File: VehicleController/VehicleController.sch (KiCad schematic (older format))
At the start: 20 parts, among them P2 BATT_IN, U1 Teensy_3.5

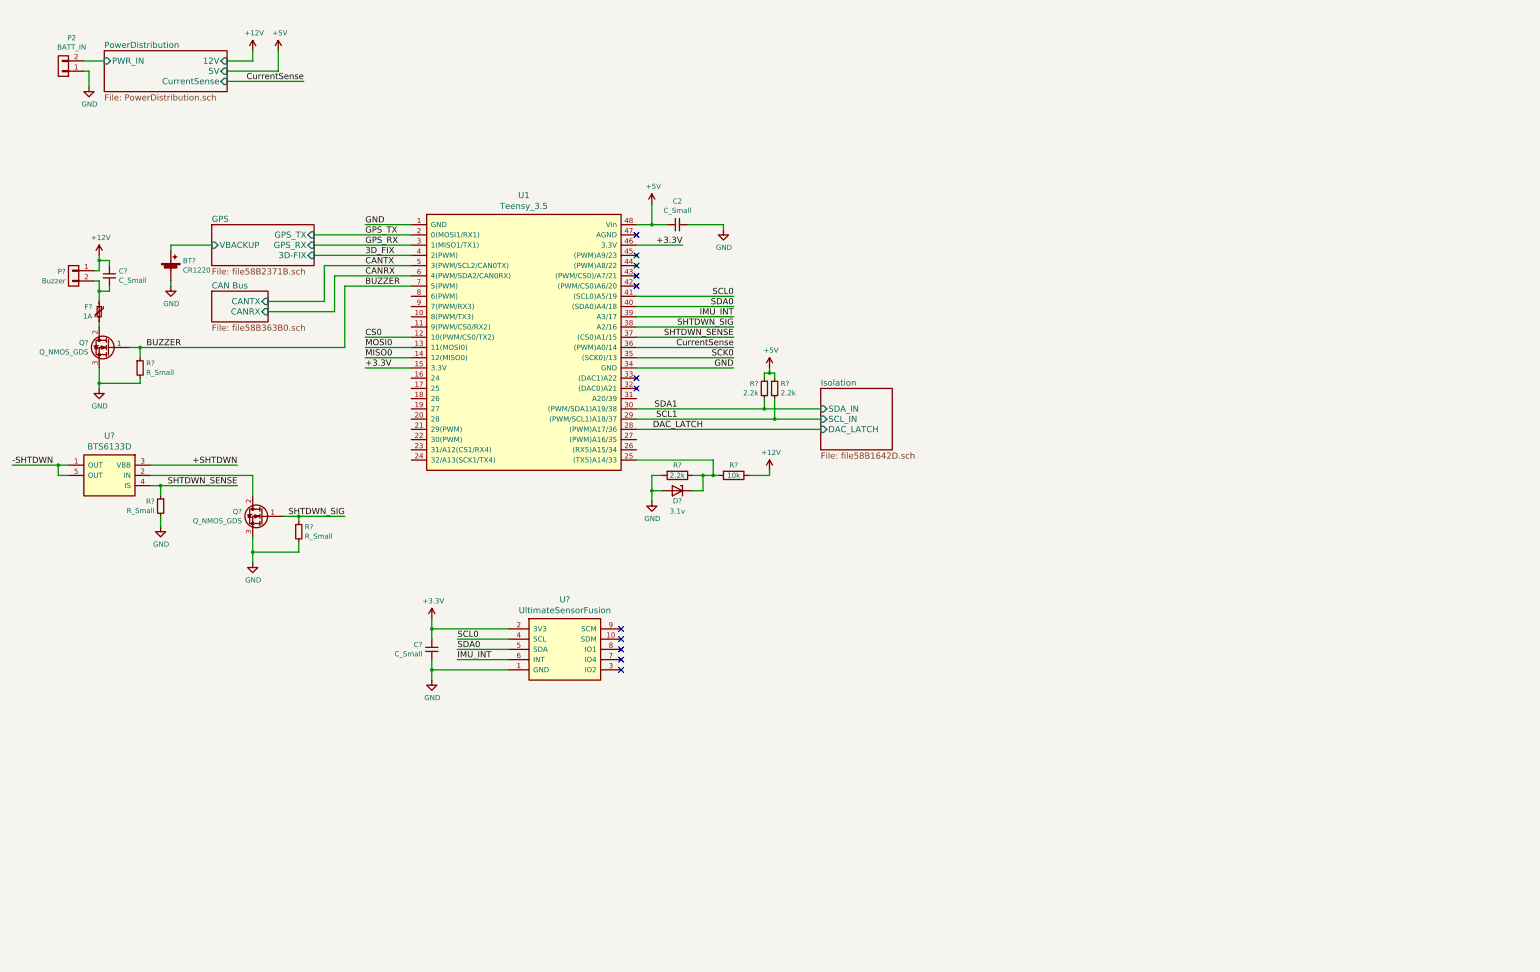
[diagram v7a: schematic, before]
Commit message: Add High-G Accel, connectors
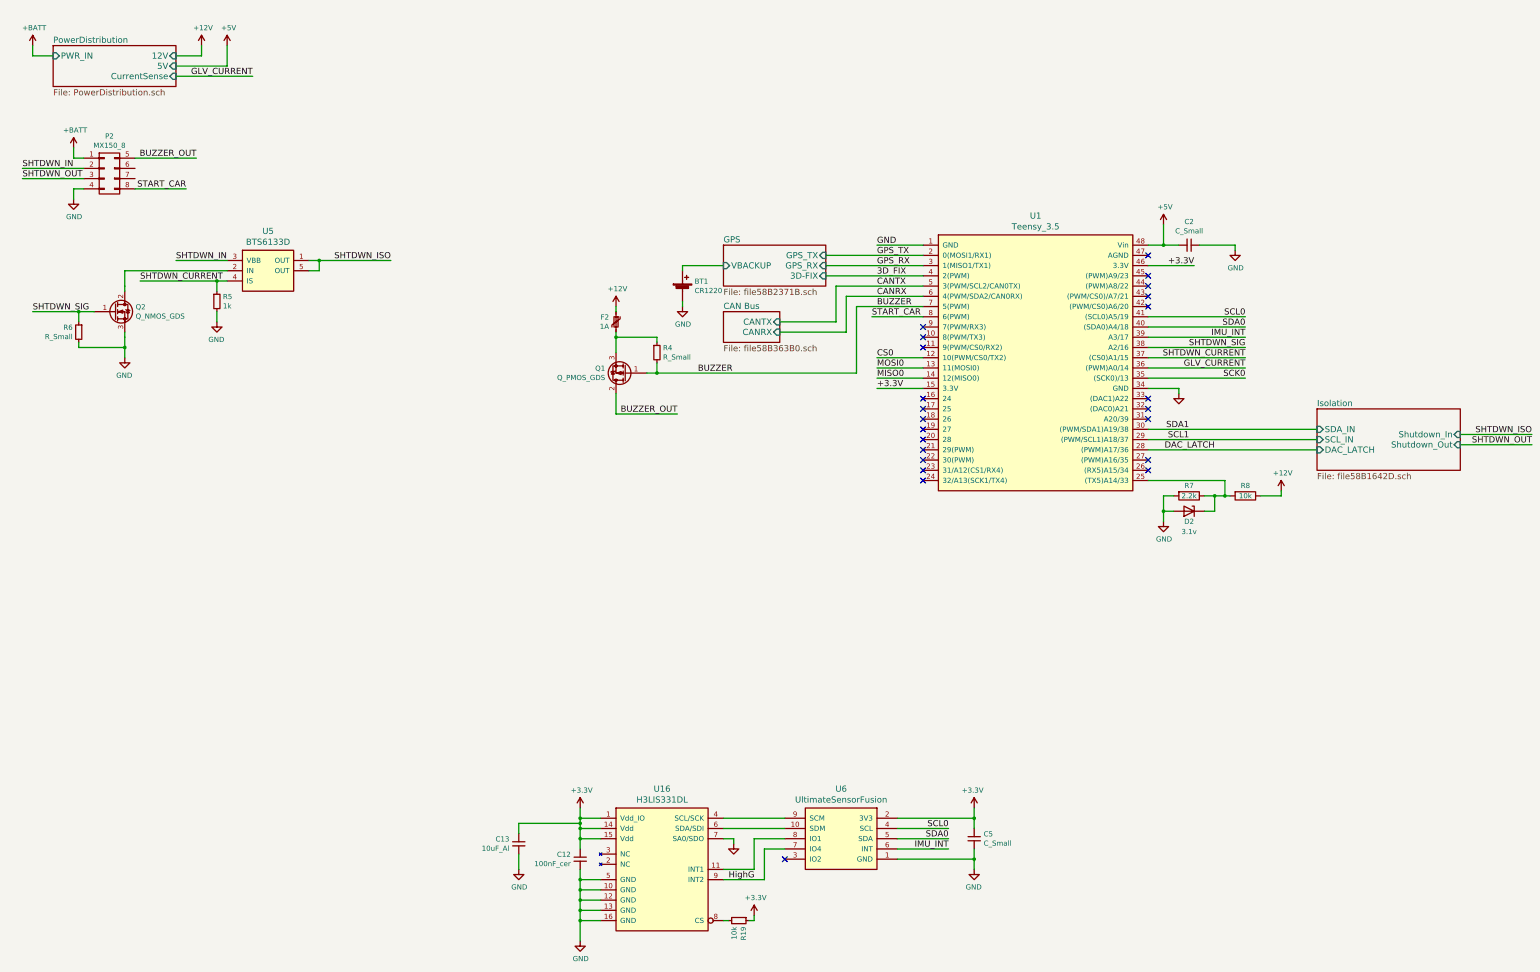
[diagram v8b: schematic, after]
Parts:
- removed C?: C_Small, symbol C_Small
- removed P2: BATT_IN, symbol CONN_01X02
- removed P?: Buzzer, symbol CONN_01X02
- removed Q?: Q_NMOS_GDS, symbol Q_NMOS_GDS
- removed R? (x2): 2.2k, symbol R_Small
- removed R?: R_Small, symbol R_Small
- added C12: 100nF_cer, symbol C_Small
- added C13: 10uF_Al, symbol C_Small
- added P2: MX150_8, symbol MX150_8
- added Q1: Q_PMOS_GDS, symbol Q_PMOS_GDS
- added R19: 10k, symbol R_Small
- added R4: R_Small, symbol R_Small
- added U16: H3LIS331DL, symbol H3LIS331DL
- R5: renamed from R?; value R_Small -> 1k
- gave numbers to parts that had none: 10
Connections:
- net +12V: now also F2.1
- net +3V3: now also C12.1, C13.1, R19.1, U16.1 (Vdd_IO), U16.14 (Vdd), U16.15 (Vdd)
- net BUZZER: now also Q1.1 (G), R4.2
- net GND: now also C12.2, C13.2, P2.4 (P7), U16.10 (GND), U16.12 (GND), U16.13 (GND), U16.16 (GND), U16.5 (GND), U16.7 (SA0/SDO)
- net START_CAR: now reaches U1.8 (6(PWM))
- net START_CAR: now also P2.8 (P8)
- net at U6.10 (SDM): now also U16.6 (SDA/SDI)
- net HighG: now reaches U6.7 (IO4)
- net HighG: now also U16.9 (INT2)
- net at U6.8 (IO1): now also U16.11 (INT1)
- net at U6.9 (SCM): now also U16.4 (SCL/SCK)
- net at F2.2: now also Q1.3 (S), R4.1
- net +SHTDWN renamed SHTDWN_IN
- net SHTDWN_IN: now also P2.2 (P3)
- net -SHTDWN renamed SHTDWN_ISO
- net CurrentSense renamed GLV_CURRENT
- net SHTDWN_SENSE renamed SHTDWN_CURRENT
- new net: R19.2, U16.8 (CS)
- new net +BATT: P2.1 (P1)
- new net BUZZER_OUT: P2.5 (P2), Q1.2 (D)
- new net SHTDWN_OUT: P2.3 (P5)
- no-connect marks 12 -> 23
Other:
- moved on the sheet: BT1, C2, C5, D2, F2, Q2, R5, R6, R7, R8, U1, U5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
